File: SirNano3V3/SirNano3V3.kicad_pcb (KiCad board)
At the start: 2 copper layers, 45.2 x 18 mm, 41 parts, among them J1 Conn_01x14, J2 Conn_01x14, J3 USB_B_Micro, U1 ATmega328PB-MU, U2 AP2210K-ADJ

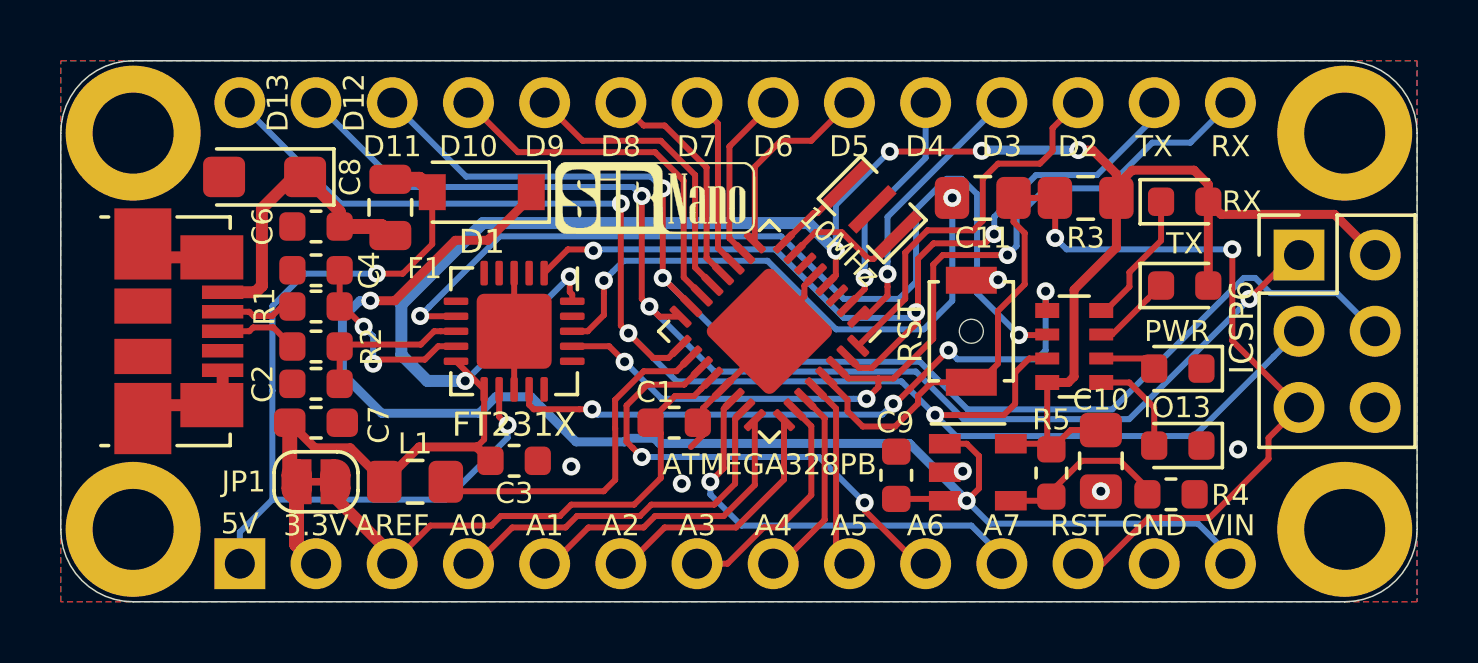
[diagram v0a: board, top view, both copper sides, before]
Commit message: Dimensions Updated
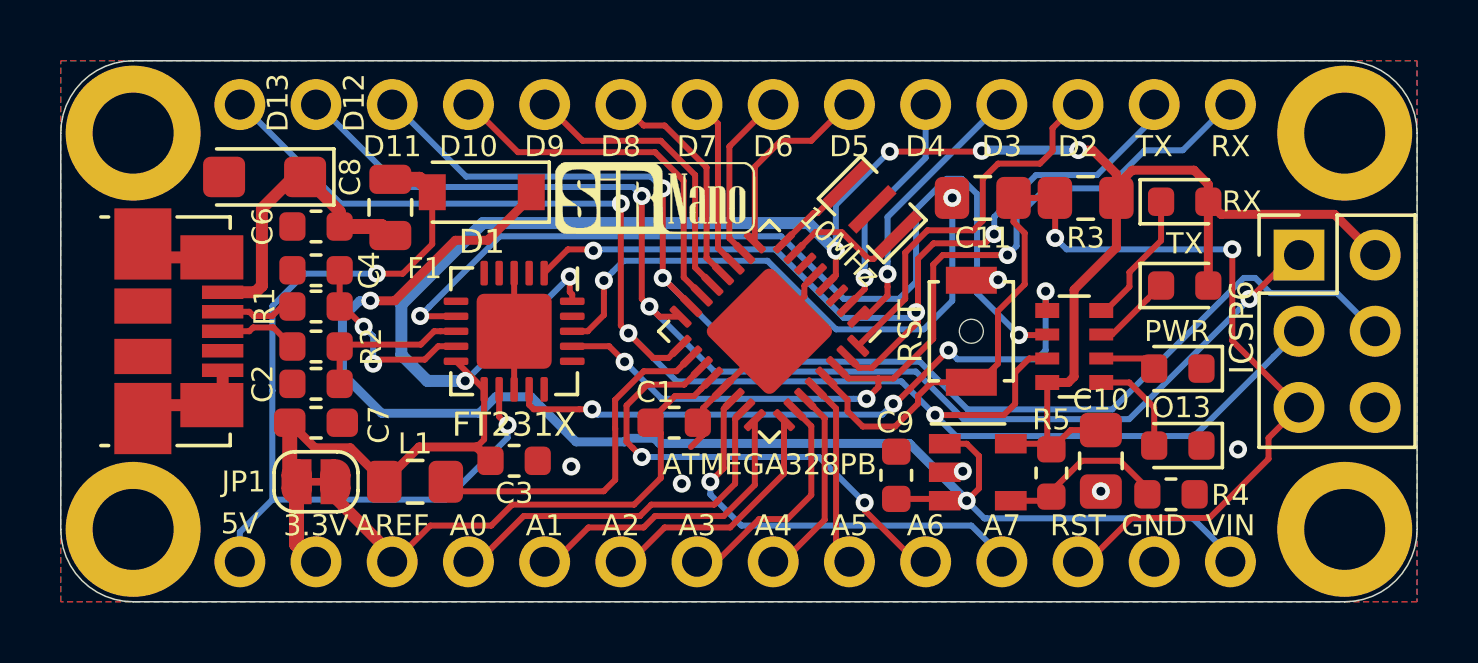
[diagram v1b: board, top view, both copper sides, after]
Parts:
- moved J1 0.06 mm to (112.8, 62.8)
- moved J2 0.06 mm to (112.8, 47.6)
